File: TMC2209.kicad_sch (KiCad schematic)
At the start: 23 parts, among them J3 Motor, U1 TMC2209-LA

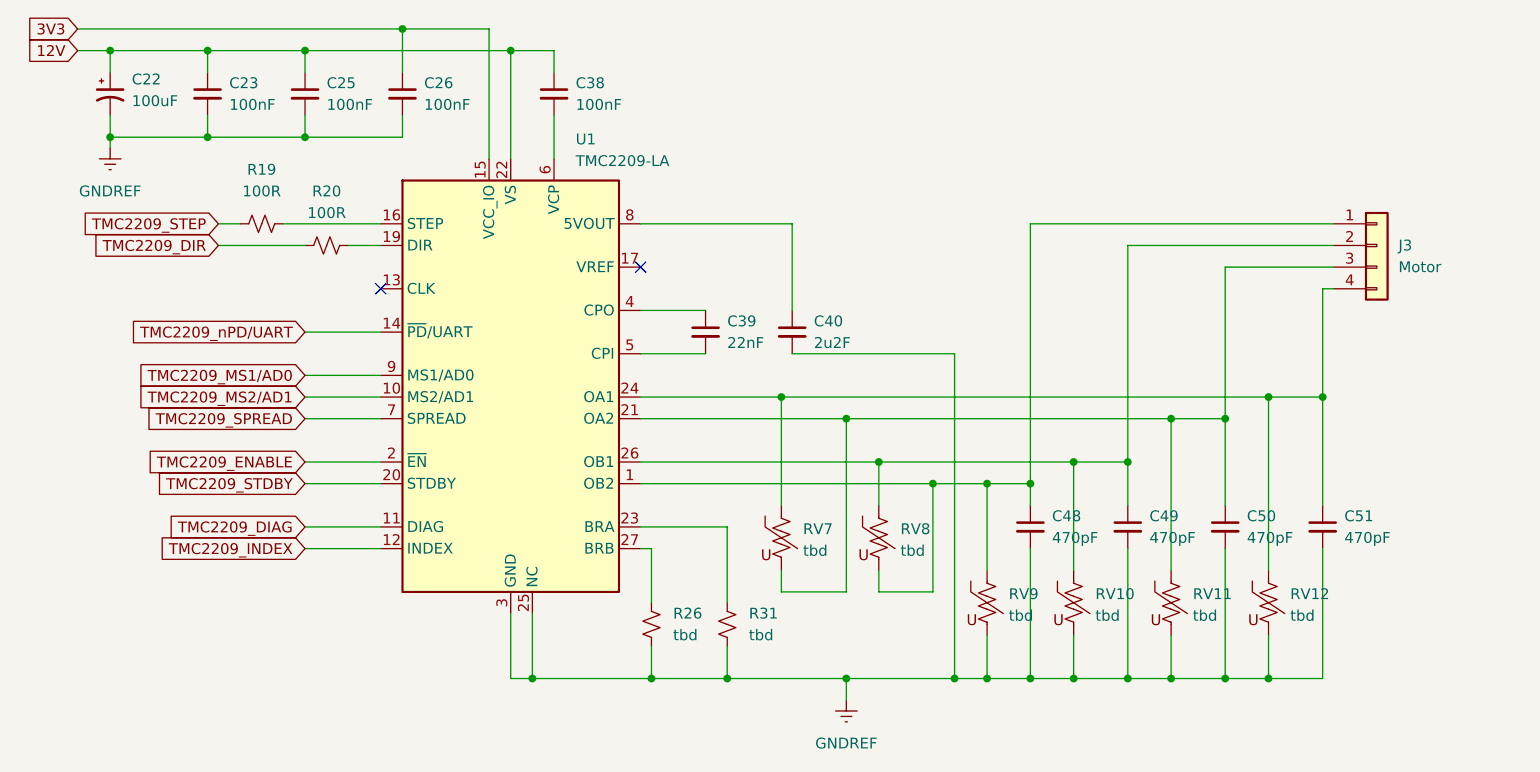
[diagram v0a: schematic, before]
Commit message: updated components and nets
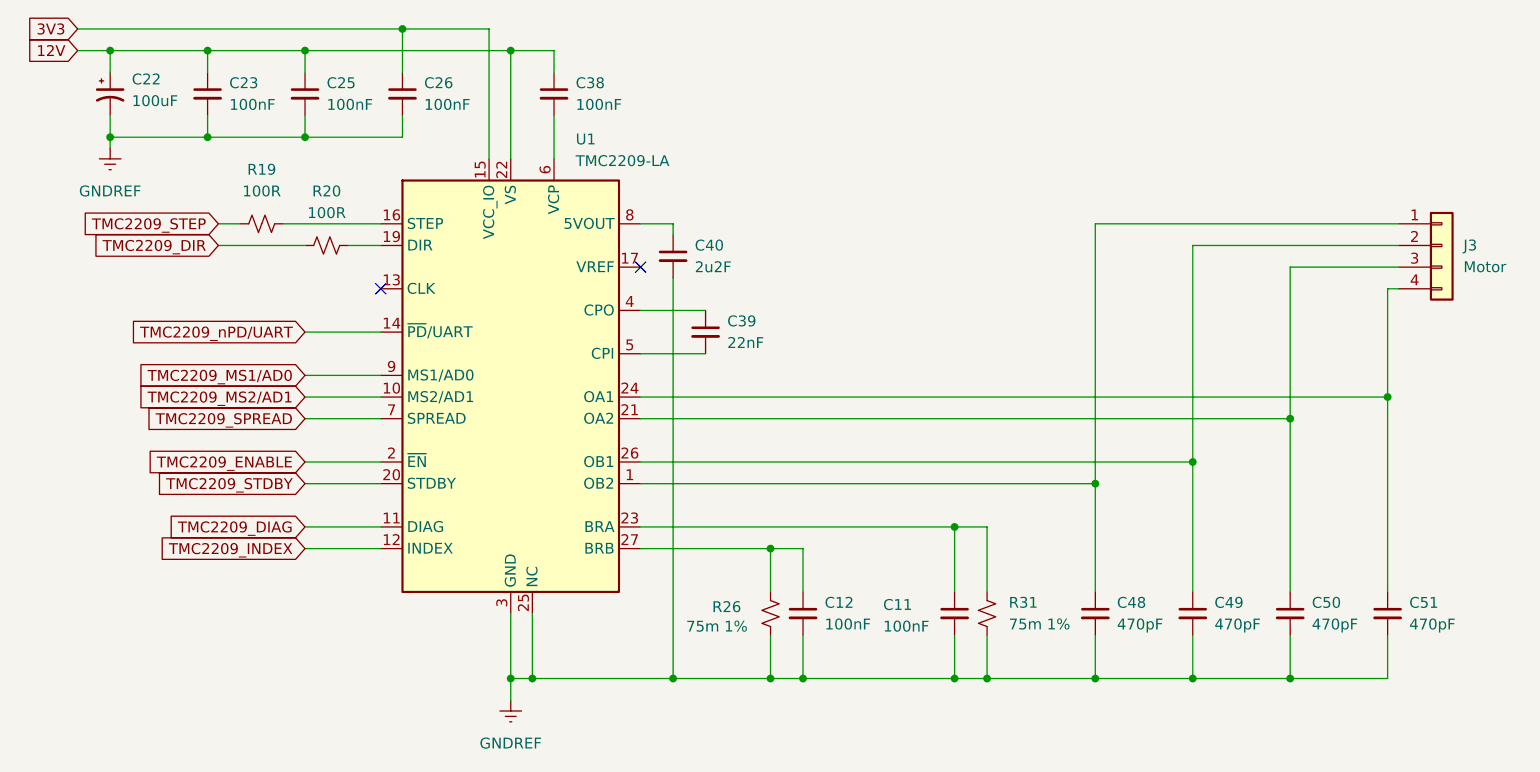
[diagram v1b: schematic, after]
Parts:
- removed RV10, RV11, RV12, RV7, RV8, RV9: tbd, symbol Device:Varistor_US
- added C11, C12: 100nF, symbol Device:C_Small
- R26, R31: value tbd -> 75m 1%
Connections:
- net GNDREF: now also C11.2, C12.2
- net at R31.1, U1.23 (BRA): now also C11.1
- net at R26.1, U1.27 (BRB): now also C12.1
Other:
- moved on the sheet: C40, C48, C49, C50, C51, J3, R26, R31

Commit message: readme file, protection on motor output
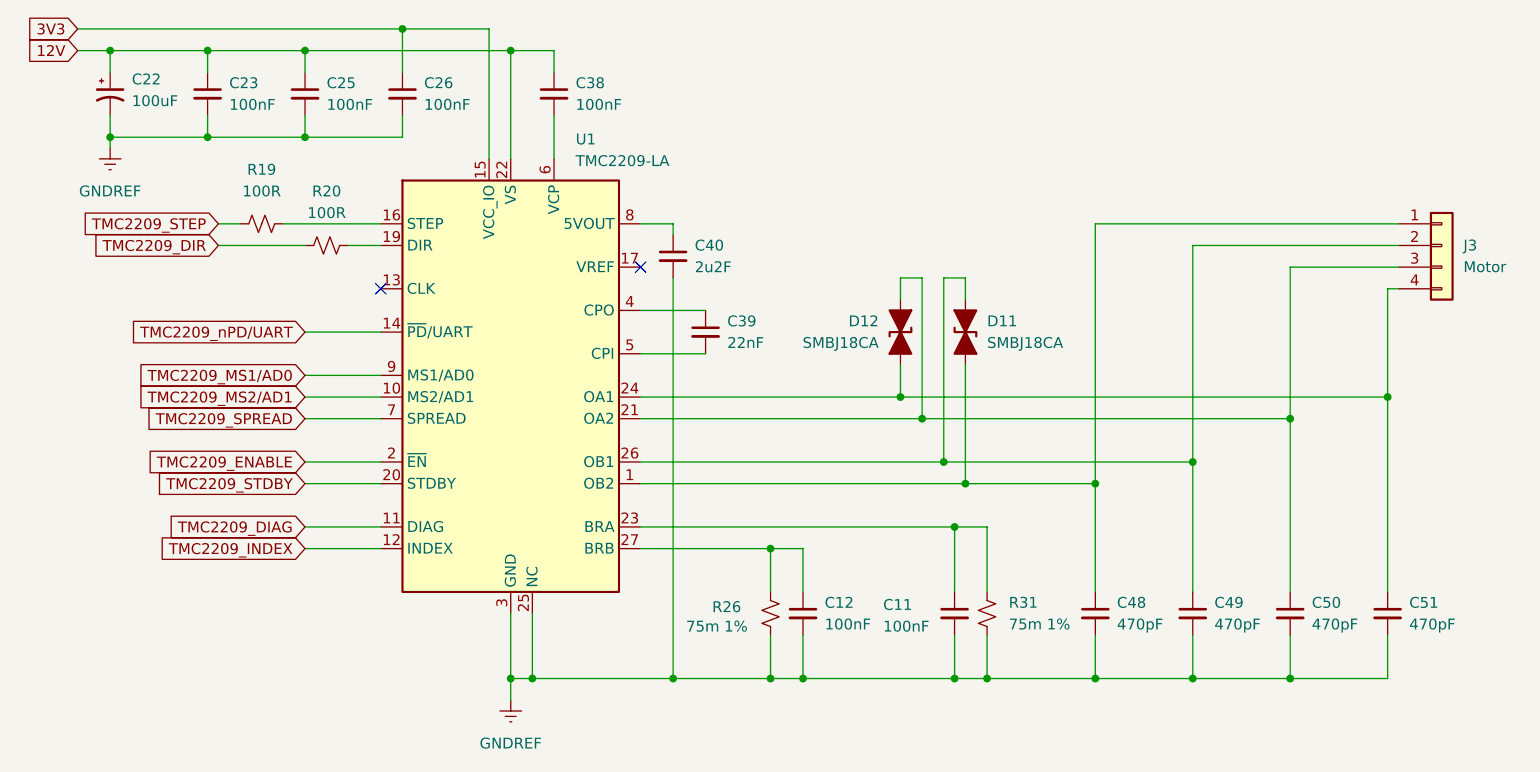
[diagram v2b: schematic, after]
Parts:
- added D11, D12: SMBJ18CA, symbol Device:D_TVS_Filled
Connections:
- net at C48.1, J3.1 (Pin_1), U1.1 (OB2): now also D11.1 (A1)
- net at C49.1, J3.2 (Pin_2), U1.26 (OB1): now also D11.2 (A2)
- net at C50.1, J3.3 (Pin_3), U1.21 (OA2): now also D12.2 (A2)
- net at C51.1, J3.4 (Pin_4), U1.24 (OA1): now also D12.1 (A1)
